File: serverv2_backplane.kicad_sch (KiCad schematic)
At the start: 0 parts

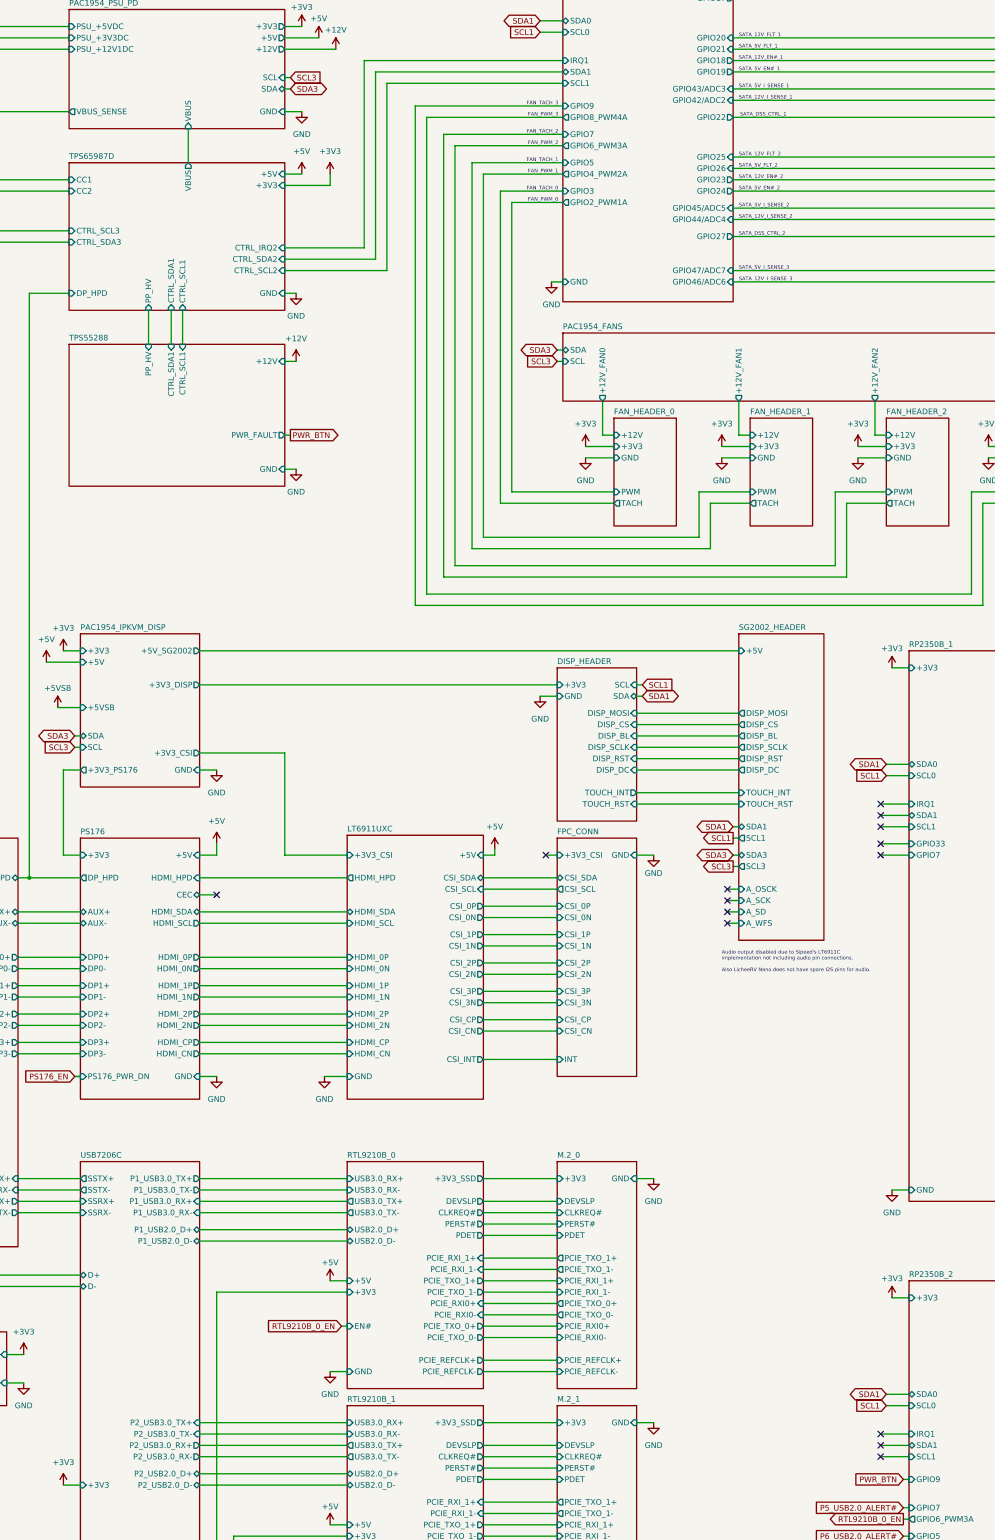
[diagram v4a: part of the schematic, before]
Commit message: Switched USB7206C IC to USB7205C
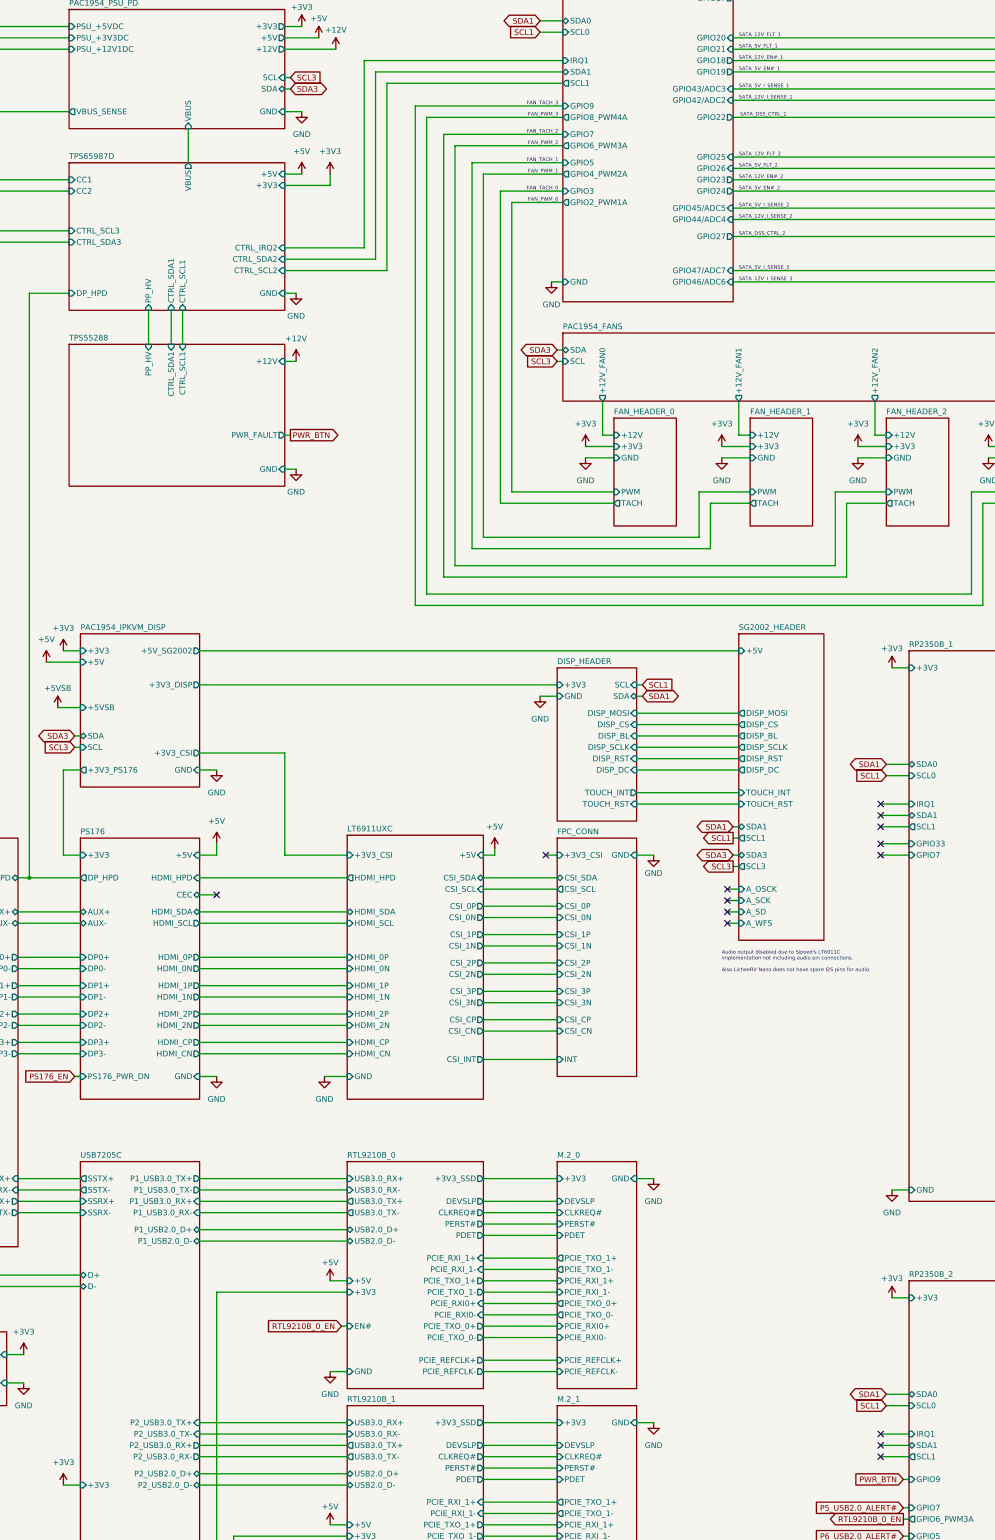
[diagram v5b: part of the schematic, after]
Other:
- sheet USB7206C renamed USB7205C
- sheet USB7205C: file USB7206C.kicad_sch -> USB7205C.kicad_sch
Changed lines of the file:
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@@
 			)
 		)
-		(pin "SCL1" input
+		(pin "SCL1" output
 			(at 278.13 226.06 180)
 			(effects
@@
 			)
 		)
-		(pin "SCL1" input
+		(pin "SCL1" output
 			(at 200.66 59.69 180)
 			(effects
@@
 			(color 0 0 0 0)
 		)
-		(property "Sheetname" "USB7206C"
+		(property "Sheetname" "USB7205C"
 			(at 92.71 300.2784 0)
 			(show_name no)
@@
 			)
 		)
-		(property "Sheetfile" "USB7206C.kicad_sch"
+		(property "Sheetfile" "USB7205C.kicad_sch"
 			(at 92.71 500.9646 0)
 			(hide yes)
@@
 			)
 		)
-		(pin "SCL1" input
+		(pin "SCL1" output
 			(at 278.13 367.03 180)
 			(effects

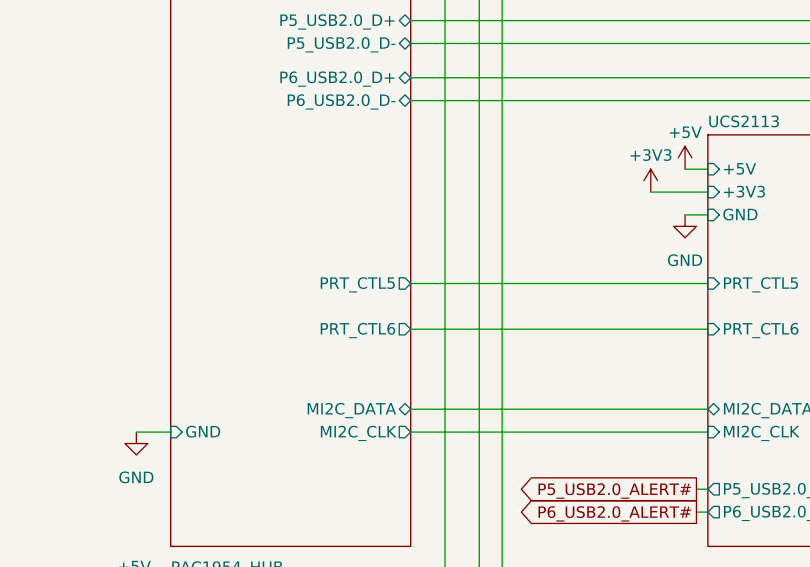
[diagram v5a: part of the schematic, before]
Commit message: Initial design of USB7205C
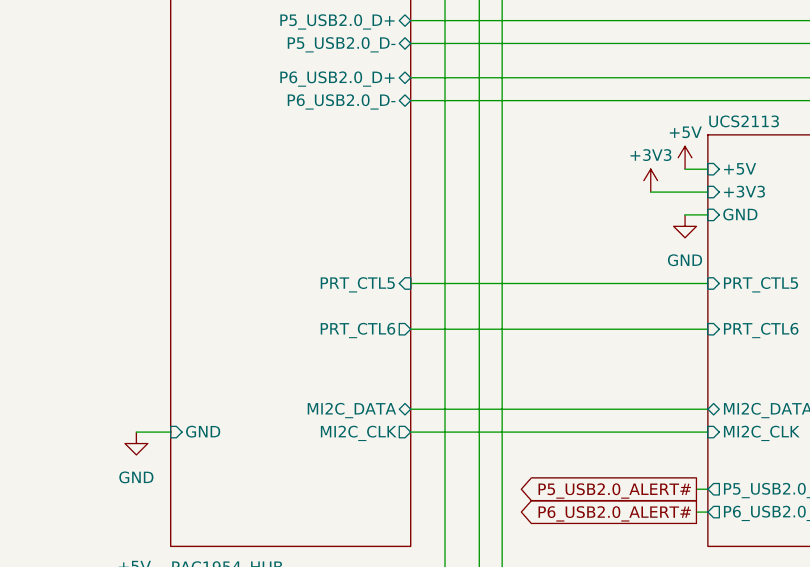
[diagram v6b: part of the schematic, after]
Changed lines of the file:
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@@
 			)
 		)
-		(pin "PRT_CTL5" output
+		(pin "PRT_CTL5" input
 			(at 119.38 471.17 0)
 			(effects

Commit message: Basic Function Review/Documentation of USB7205C
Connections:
- no-connect marks 15 -> 13
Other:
- sheet PORT6_USB renamed PORT4_USB
- sheet PORT4_USB: file PORT6_USB.kicad_sch -> PORT4_USB.kicad_sch
- sheet UCS2113 ports: added P4_USB2.0_ALERT#, P4_USB2.0_VCC, PRT_CTL4; removed P6_USB2.0_ALERT#, P6_USB2.0_VCC, PRT_CTL6
- sheet USB7205C ports: added P4_USB2.0_D+, P4_USB2.0_D-, PRT_CTL4, SI2C_SCL, SI2C_SDA; removed P6_USB2.0_D+, P6_USB2.0_D-, PRT_CTL6
